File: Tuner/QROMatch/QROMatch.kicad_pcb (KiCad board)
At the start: 2 copper layers, 200 x 100 mm, 160 parts, among them J1 Conn_02x12_Odd_Even, J10 Conn_02x12_Odd_Even, J11 Conn_01x01, J12 Conn_01x01, J13 Conn_01x01, J14 Conn_01x01, J2 Conn_01x06, J3 Conn_01x06

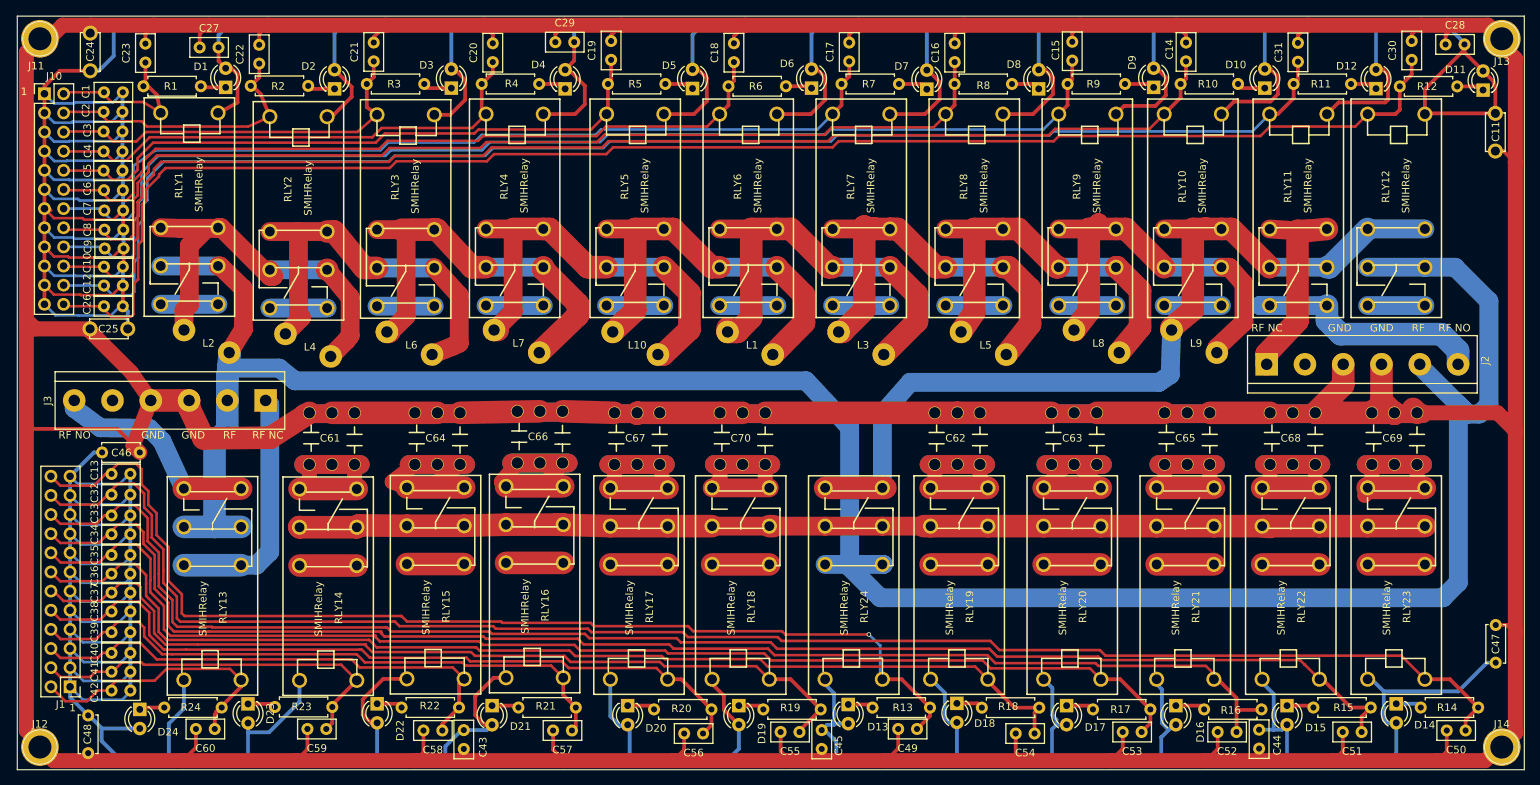
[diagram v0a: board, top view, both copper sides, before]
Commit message: Changed capacitance high-Z low-Z to have less series inductance
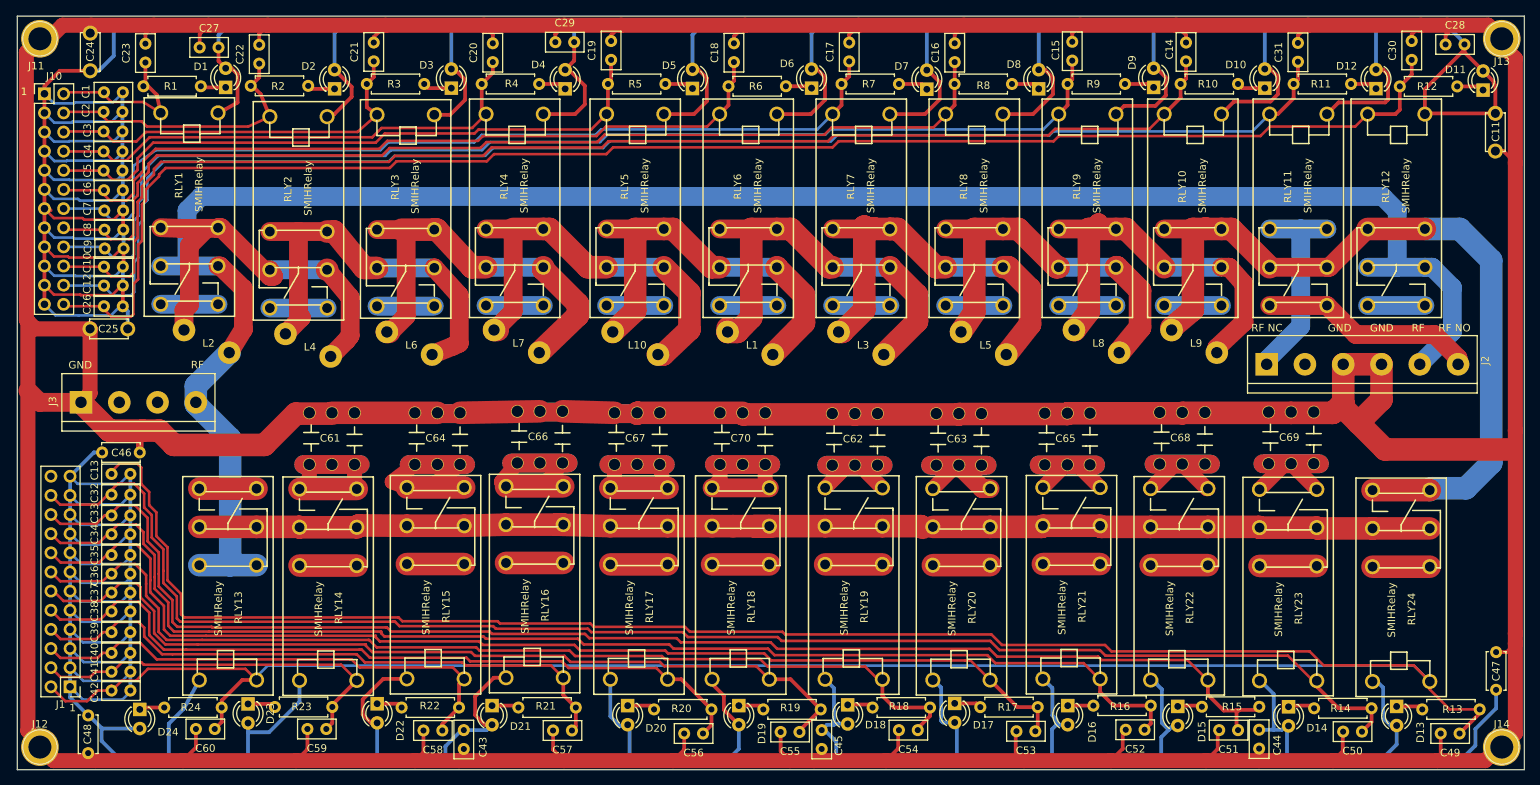
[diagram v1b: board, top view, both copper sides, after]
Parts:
- J3: value Conn_01x06 -> Conn_01x04; footprint Connectors_Terminal_Blocks:TerminalBlock_bornier-6_P5.08mm -> Connectors_Terminal_Blocks:TerminalBlock_bornier-4_P5.08mm
- moved R13 73.0 mm to (216.4, 122.0)
- moved D13 72.8 mm to (213.1, 121.6)
- moved RLY24 72.7 mm to (213.7, 108.3)
- moved C49 72.0 mm to (221.4, 125.2)
- moved J3 24.5 mm to (38.5, 81.2), turned to 0 degrees
- moved C51 16.4 mm to (192.0, 124.8)
- moved C65 15.9 mm to (169.6, 86.0)
- moved C54 15.5 mm to (149.5, 124.8)
- moved C63 15.3 mm to (155.2, 86.1)
- moved RLY21 15.1 mm to (169.9, 108.0)
- moved R17 15.0 mm to (157.8, 121.7)
- moved D17 14.9 mm to (154.4, 121.2)
- moved R15 14.8 mm to (187.2, 121.7)
- moved RLY22 14.8 mm to (184.2, 108.1)
- moved R16 14.7 mm to (172.8, 121.5)
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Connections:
- C13 pad 1: RLY24 -> RLY13
- C49 pad 1: RLY24 -> RLY13
- J1 pad 24: RLY24 -> (no net)
- J3 pad 1: Net-(J3-Pad1) -> RFGND
- J3 pad 2: RFSIG -> (no net)
- J3 pad 3: RFGND -> (no net)
- J3 pad 4: RFGND -> RFSIG
- R13 pad 2: RLY24 -> RLY13
- RLY13 pad 1: RFSIG -> RFCAP
- RLY13 pad 2: Net-(J3-Pad1) -> RFSIG
- RLY13 pad 3: Net-(J3-Pad6) -> Net-(RLY13-Pad3)
- RLY24 pad 2: RFSIG -> Net-(RLY24-Pad2)
- RLY24 pad 5: RLY24 -> RLY13
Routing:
- net RLY13: track 37.9 -> 407.7 mm
- net RLY24: track 146.2 -> 0.00 mm, vias 1 -> 0
- net RFSIG: track 318.0 -> 262.6 mm
- net Net-(J3-Pad1): track 32.5 -> 0.00 mm
- net Net-(J3-Pad6): track 28.8 -> 0.00 mm
- net RFGND: track 908.3 -> 934.0 mm
- net RLY20: track 165.0 -> 149.8 mm
- net RFCAP: track 153.9 -> 169.0 mm
- net RLY21: track 182.4 -> 167.7 mm
- net RLY23: track 214.6 -> 200.9 mm
- net RLY22: track 197.9 -> 184.3 mm
- net RLY19: track 147.8 -> 134.3 mm
- net RFOUT: track 119.9 -> 110.4 mm
- net Net-(RLY13-Pad3): track 0.00 -> 7.60 mm
- net Net-(RLY24-Pad2): track 0.00 -> 7.60 mm
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
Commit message: Added extra capacitors between relay power and ground posts
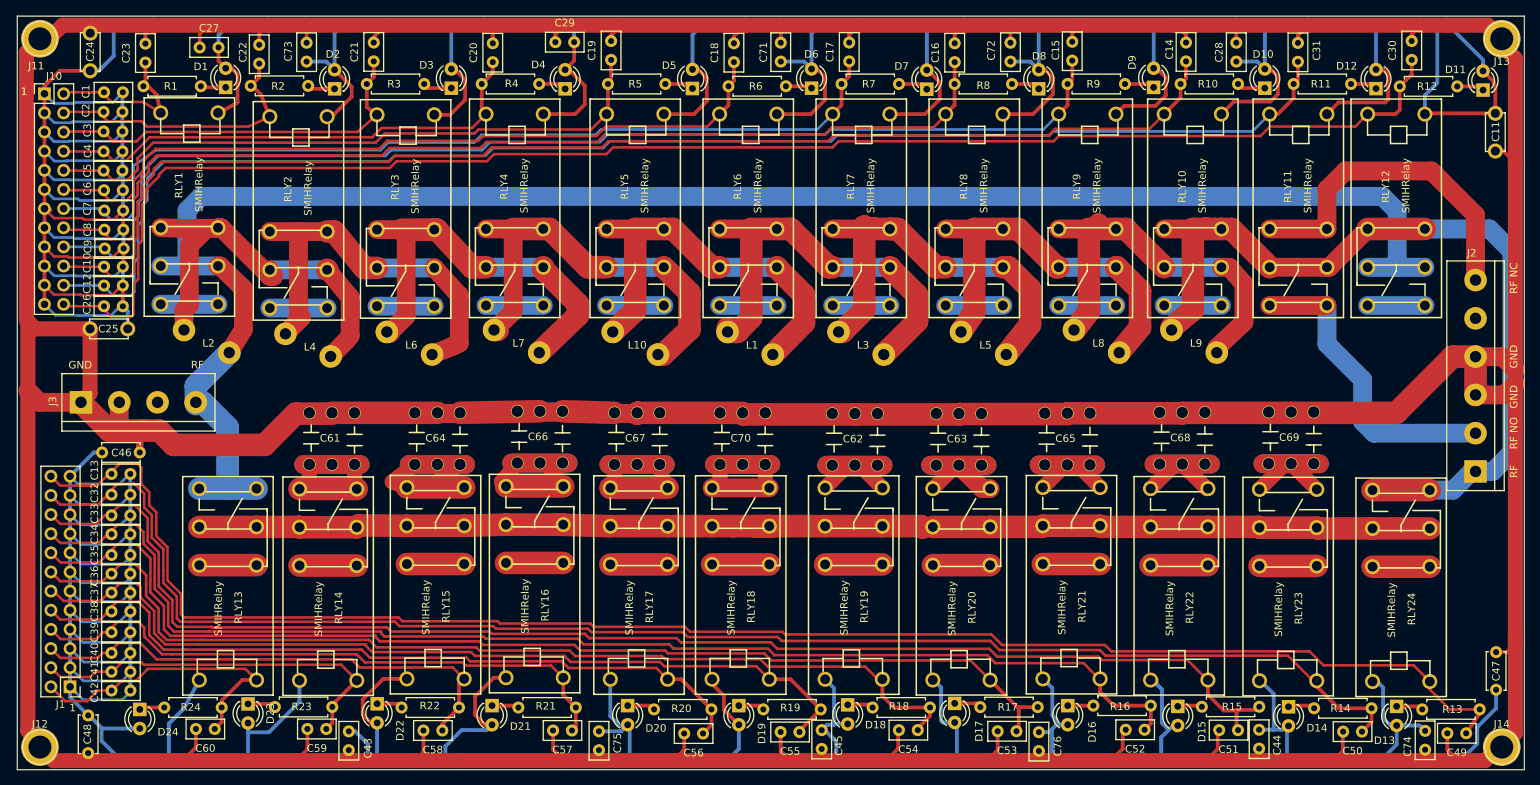
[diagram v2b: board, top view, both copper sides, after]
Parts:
- added C71: 10 nF, Capacitors_THT:C_Disc_D5.0mm_W2.5mm_P2.50mm, F.Cu at (131.3, 33.5)
- added C72: 10 nF, Capacitors_THT:C_Disc_D5.0mm_W2.5mm_P2.50mm, F.Cu at (161.8, 33.5)
- added C73: 10 nF, Capacitors_THT:C_Disc_D5.0mm_W2.5mm_P2.50mm, F.Cu at (68.4, 33.5)
- added C74: 10 nF, Capacitors_THT:C_Disc_D5.0mm_W2.5mm_P2.50mm, F.Cu at (216.8, 127.3)
- added C75: 10 nF, Capacitors_THT:C_Disc_D5.0mm_W2.5mm_P2.50mm, F.Cu at (107.2, 127.4)
- added C76: 10 nF, Capacitors_THT:C_Disc_D5.0mm_W2.5mm_P2.50mm, F.Cu at (165.6, 127.5)
- moved J2 31.2 mm to (223.5, 90.4), turned to 90 degrees
- moved C28 27.8 mm to (191.8, 33.5), turned to 270 degrees
- moved C43 15.3 mm to (74.0, 127.4)
- moved C53 2.50 mm to (162.6, 124.9)
- moved C49 0.88 mm to (222.3, 125.2)
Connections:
- C13 pad 1: RLY13 -> RLY24
- C49 pad 1: RLY13 -> RLY24
- J1 pad 24: (no net) -> RLY24
- J2 pad 1: Net-(J2-Pad1) -> RFOUT
- J2 pad 2: (no net) -> Net-(J2-Pad2)
- J2 pad 5: RFSIG -> (no net)
- J3 pad 2: (no net) -> RFGND
- R13 pad 2: RLY13 -> RLY24
- RLY11 pad 2: Net-(J2-Pad1) -> Net-(J2-Pad6)
- RLY11 pad 3: Net-(J2-Pad6) -> Net-(J2-Pad2)
- RLY13 pad 2: RFSIG -> Net-(RLY13-Pad2)
- RLY13 pad 3: Net-(RLY13-Pad3) -> RFSIG
- RLY24 pad 5: RLY13 -> RLY24
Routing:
- net RLY13: track 407.7 -> 41.5 mm
- net RLY24: track 0.00 -> 217.7 mm
- net Net-(J2-Pad2): track 0.00 -> 40.6 mm
- net Net-(J2-Pad1): track 27.4 -> 0.00 mm
- net RFSIG: track 262.6 -> 235.9 mm
- net +5V: track 621.4 -> 639.8 mm
- net Net-(J2-Pad6): track 28.7 -> 44.6 mm
- net +12V: track 557.7 -> 573.4 mm
- net RFGND: track 934.0 -> 947.3 mm
- net Net-(RLY13-Pad3): track 7.60 -> 0.00 mm
- net Net-(RLY13-Pad2): track 0.00 -> 7.60 mm
- net RFOUT: track 110.4 -> 115.7 mm

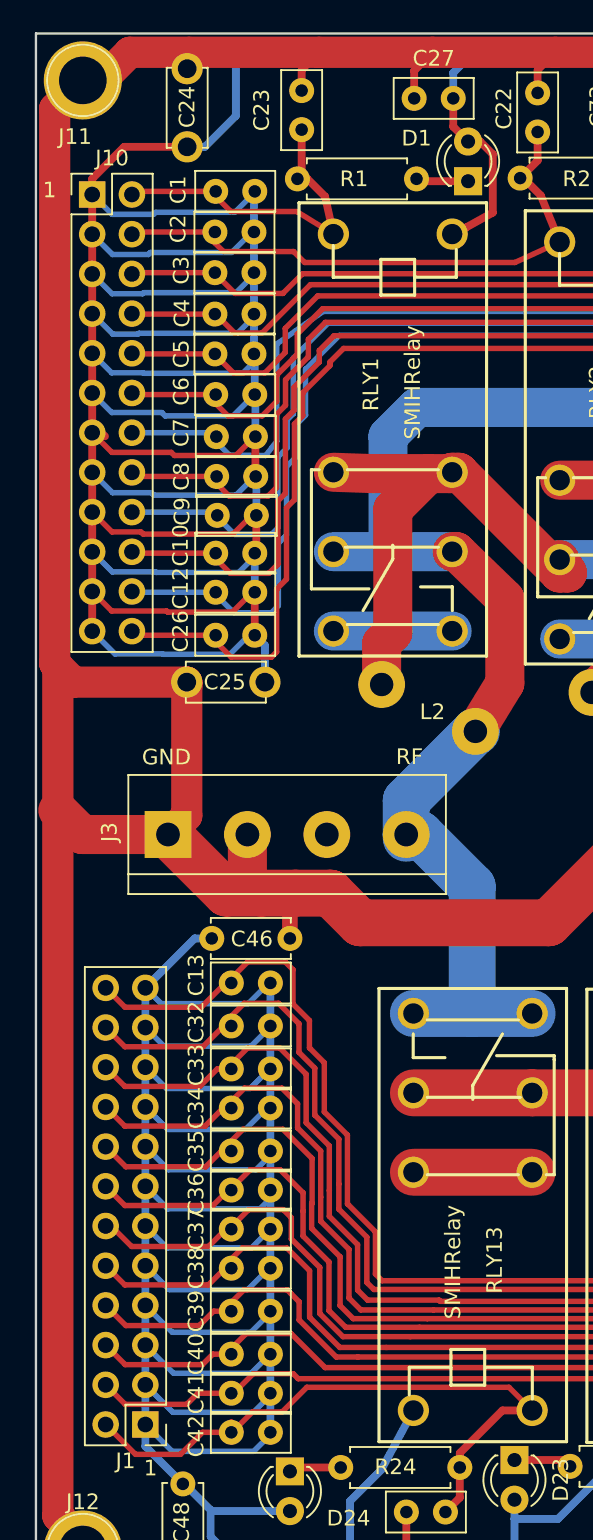
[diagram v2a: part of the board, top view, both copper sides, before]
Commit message: Changed from 2x12 IDC to more common 2x13 IDC
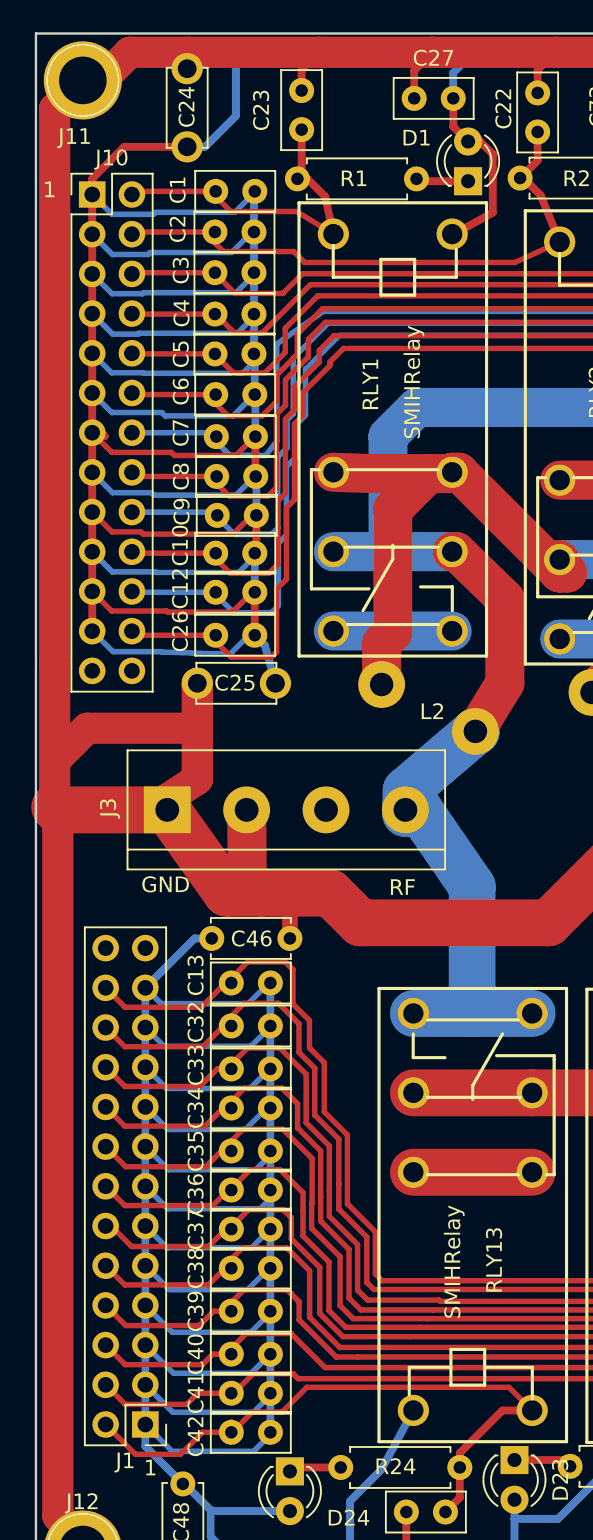
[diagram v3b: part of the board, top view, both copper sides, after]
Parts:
- J1, J10: value Conn_02x12_Odd_Even -> Conn_02x13_Odd_Even; footprint Pin_Headers:Pin_Header_Straight_2x12_Pitch2.54mm -> Pin_Headers:Pin_Header_Straight_2x13_Pitch2.54mm
- moved J3 1.58 mm to (38.4, 79.7)
- moved C25 0.68 mm to (40.3, 71.6)
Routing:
- net RFGND: track 947.3 -> 949.6 mm
